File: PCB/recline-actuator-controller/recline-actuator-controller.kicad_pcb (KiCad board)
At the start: 4 copper layers, 140 x 100 mm, 171 parts, among them J1 DX07S016JA1R1500, J10 1757242, J11 1757242, J12 0705430002, J13 0705430002, J14 0705430002, J15 0705430002, J16 1757242, J17 1757242, J18 0705430002, J19 0705430002, J2 Conn_01x03, J20 0705430002, J21 0705430002, J22 1757242, J3 RJSAE-538A-02, J4 1757242, J5 1757242, J6 1757242, J7 1757242, J8 1757242, J9 1757242, M2 D24V22F3, Q1 PSMN7R0-60YS,115, Q2 PSMN7R0-60YS,115, Q3 PSMN7R0-60YS,115, Q4 PSMN7R0-60YS,115, Q5 PSMN7R0-60YS,115, Q6 BSC014N04LSIATMA1, Q7 BSC014N04LSIATMA1, Q8 BSC014N04LSIATMA1, Q9 BSC014N04LSIATMA1, SW1 TL3330AF260QG, SW2 TL3330AF260QG, U1 TEMPLATE, U2 RP2040, U3 MAX3535ECWI+T, U4 VNH5019ATR-E, U5 VNH5019ATR-E, U6 VNH5019ATR-E, U7 VNH5019ATR-E, U8 MCP23S17T-E/ML, X1 ABM8G-12.000MHZ-18-D2Y-T

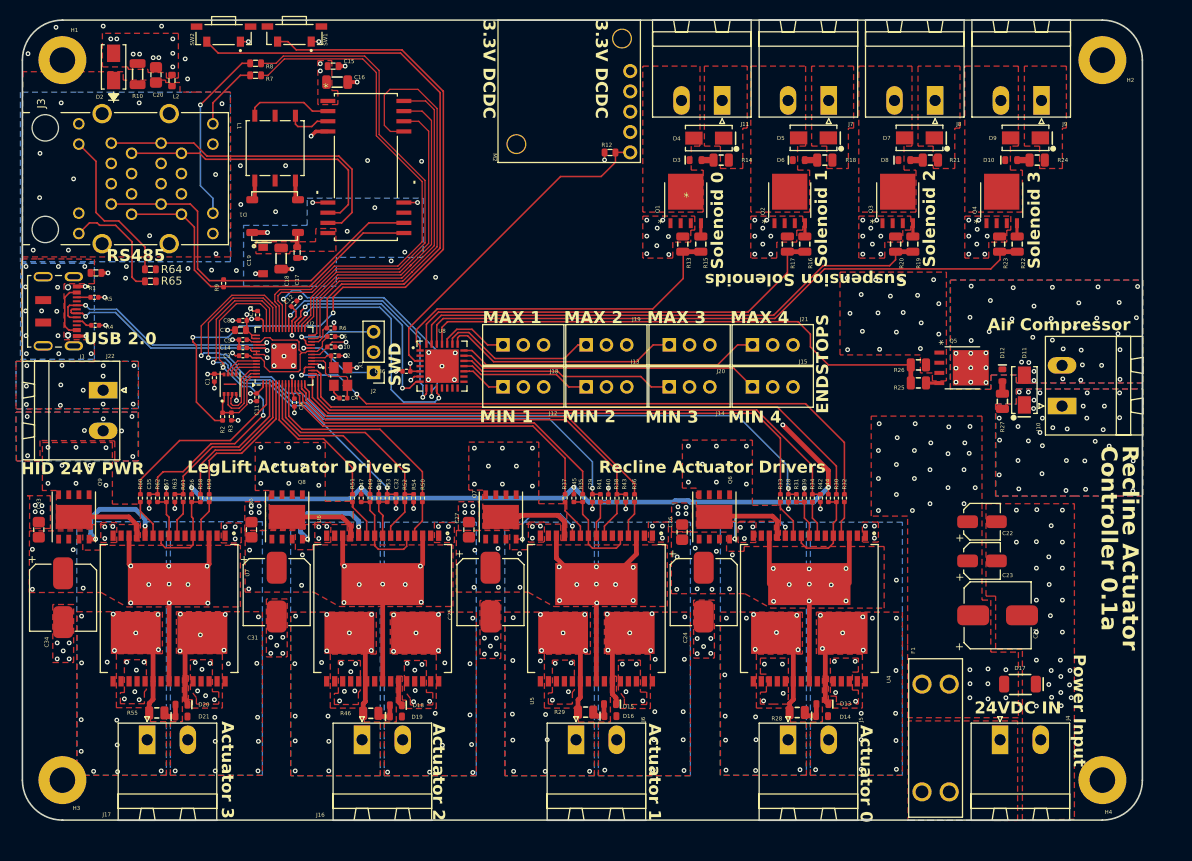
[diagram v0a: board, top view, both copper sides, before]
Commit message: Via Stichign and Pullups
Added optional pullups to endstop circuit.  Revised via stitching for input power, revised layout with added via stitching and copper pours for solenoid mosfets.
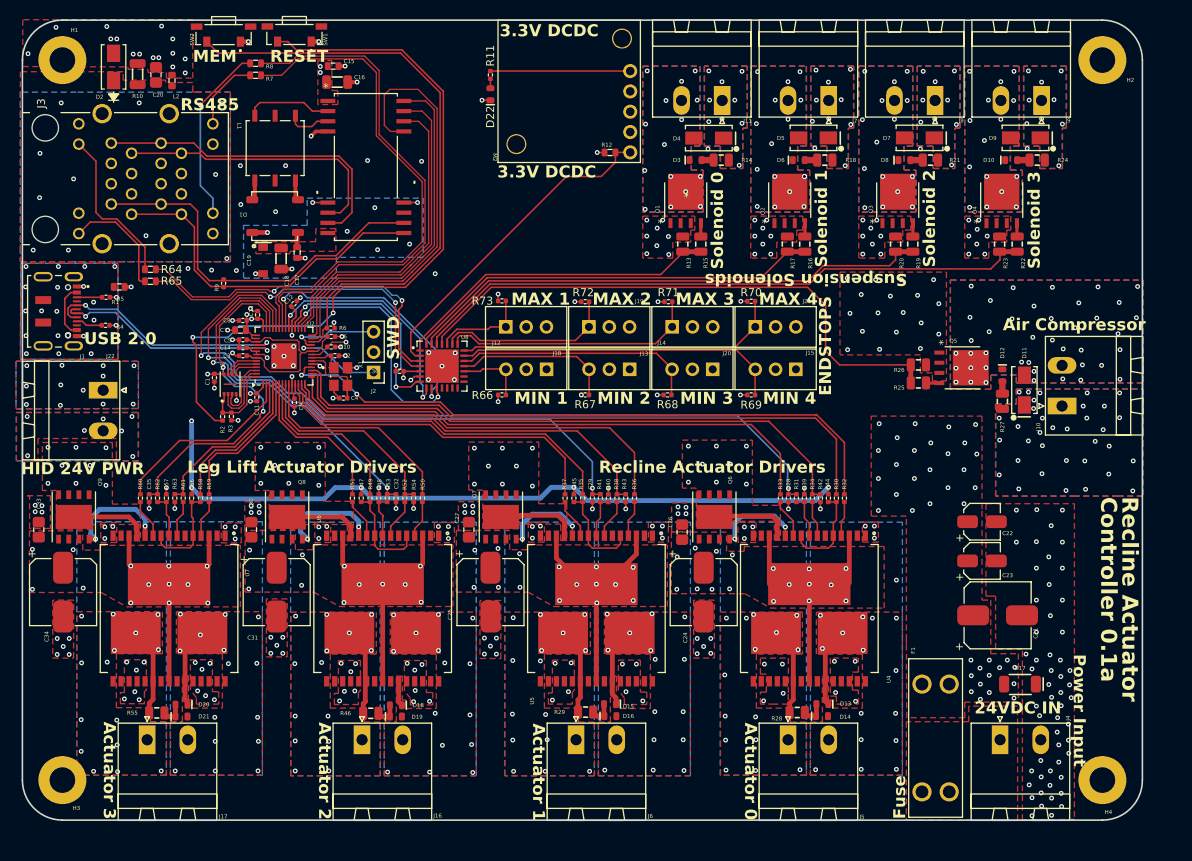
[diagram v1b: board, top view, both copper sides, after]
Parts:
- added D22: LTST-C194TBKT, AVR-KiCAD-Lib-Diodes:LED0603, F.Cu at (108.5, 54.3)
- added R11: RC0402FR-071KL, AVR-KiCAD-Lib-Resistors:R0402, F.Cu at (108.5, 51.9)
- added R66: RC0402FR-0710KL, AVR-KiCAD-Lib-Resistors:R0402, F.Cu at (110.0, 91.8)
- added R67: RC0402FR-0710KL, AVR-KiCAD-Lib-Resistors:R0402, F.Cu at (120.3, 91.8)
- added R68: RC0402FR-0710KL, AVR-KiCAD-Lib-Resistors:R0402, F.Cu at (130.7, 91.8)
- added R69: RC0402FR-0710KL, AVR-KiCAD-Lib-Resistors:R0402, F.Cu at (141.1, 91.8)
- added R70: RC0402FR-0710KL, AVR-KiCAD-Lib-Resistors:R0402, F.Cu at (141.1, 80.2)
- added R71: RC0402FR-0710KL, AVR-KiCAD-Lib-Resistors:R0402, F.Cu at (130.8, 80.2)
- added R72: RC0402FR-0710KL, AVR-KiCAD-Lib-Resistors:R0402, F.Cu at (120.3, 80.2)
- added R73: RC0402FR-0710KL, AVR-KiCAD-Lib-Resistors:R0402, F.Cu at (110.0, 80.1)
- moved J12 5.87 mm to (115.5, 88.7), turned to -90 degrees
- moved J13 5.87 mm to (125.9, 88.7), turned to -90 degrees
- moved J14 5.87 mm to (136.3, 88.7), turned to -90 degrees
- moved J15 5.87 mm to (146.7, 88.7), turned to -90 degrees
- moved R1 3.39 mm to (62.1, 78.3)
- moved J18 2.28 mm to (110.4, 83.3)
- moved J21 2.28 mm to (141.6, 83.3)
- moved J19 2.28 mm to (120.8, 83.3)
- moved J20 2.28 mm to (131.2, 83.3)
- moved R5 1.45 mm to (60.5, 79.7)
- moved R4 1.30 mm to (60.4, 83.2)
- moved C36 0.85 mm to (97.2, 88.9)
- moved C34 0.70 mm to (55.1, 116.5)
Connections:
- J12 pad 1: /End Stop Limit Switches/MIN1 -> +3.3V
- J12 pad 3: +3.3V -> /End Stop Limit Switches/MIN1
- J13 pad 1: /End Stop Limit Switches/MIN2 -> +3.3V
- J13 pad 3: +3.3V -> /End Stop Limit Switches/MIN2
- J14 pad 1: /End Stop Limit Switches/MIN3 -> +3.3V
- J14 pad 3: +3.3V -> /End Stop Limit Switches/MIN3
- J15 pad 1: /End Stop Limit Switches/MIN4 -> +3.3V
- J15 pad 3: +3.3V -> /End Stop Limit Switches/MIN4
- R64 pad 2: /RS485 Transceiver/RS485_TX_LED2 -> /End Stop Limit Switches/RS485_TX_LED2
- R65 pad 2: /RS485 Transceiver/RS485_RX_LED2 -> /End Stop Limit Switches/RS485_RX_LED2
- U8 pad 2: /End Stop Limit Switches/5V_PG -> /Power/3.3V_PG
- U8 pad 3: /Power/3.3V_PG -> /End Stop Limit Switches/RS485_TX_LED2
- U8 pad 4: unconnected-(U8-GPB7-Pad4) -> /End Stop Limit Switches/RS485_RX_LED2
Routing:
- net /End Stop Limit Switches/RS485_TX_LED2: track 0.00 -> 43.1 mm, vias 0 -> 2
- net /End Stop Limit Switches/RS485_RX_LED2: track 0.00 -> 42.4 mm, vias 0 -> 2
- net +3.3V: track 128.6 -> 150.4 mm, vias 19 -> 27
- net /End Stop Limit Switches/AIR_COMP: track 66.5 -> 71.8 mm
- net /End Stop Limit Switches/MIN2: track 16.4 -> 20.0 mm
- net /End Stop Limit Switches/MIN3: track 27.0 -> 30.4 mm
- net /End Stop Limit Switches/SOLENOID_0: track 44.4 -> 41.1 mm
- net /End Stop Limit Switches/MIN4: track 37.7 -> 40.9 mm
- net /End Stop Limit Switches/MAX4: track 37.8 -> 40.8 mm
- net /End Stop Limit Switches/MAX1: track 8.93 -> 11.9 mm
- net /End Stop Limit Switches/MIN1: track 5.69 -> 8.57 mm
- net /End Stop Limit Switches/SOLENOID_1: track 55.1 -> 52.5 mm
- net /End Stop Limit Switches/MAX2: track 19.8 -> 22.4 mm
- net /End Stop Limit Switches/MAX3: track 29.6 -> 32.2 mm
- net /Motor H-Bridges/M2INA: track 48.5 -> 50.8 mm
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- added copper zone on In1.Cu, net Net-(F1-Pad2)
- added copper zone on B.Cu, net Net-(Q1-D)
- added copper zone on In1.Cu, net Net-(Q1-D)
- added copper zone on B.Cu, net Net-(Q2-D)
- added copper zone on In1.Cu, net Net-(Q2-D)
- added copper zone on B.Cu, net Net-(Q3-D)
- added copper zone on In1.Cu, net Net-(Q3-D)
- added copper zone on B.Cu, net Net-(Q4-D)
- added copper zone on In1.Cu, net Net-(Q4-D)
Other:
- board text added: "3V3"
- board text added: "Fuse"
- board text added: "GPA0"
- board text added: "GPA1"
- board text added: "GPA2"
- board text added: "GPA3"
- board text added: "GPA4"
- board text added: "GPA5"
- board text added: "GPA6"
- board text added: "GPA7"
- board text added: "Leg Lift Actuator Drivers"
- board text added: "MEM"
- board text added: "NOTE: ALL ON IO EXPANDER"
- board text added: "RESET"
- board text removed: "LegLift Actuator Drivers"

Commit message: Powerplane
Recline actuator controller power plane topology modified and upgraded
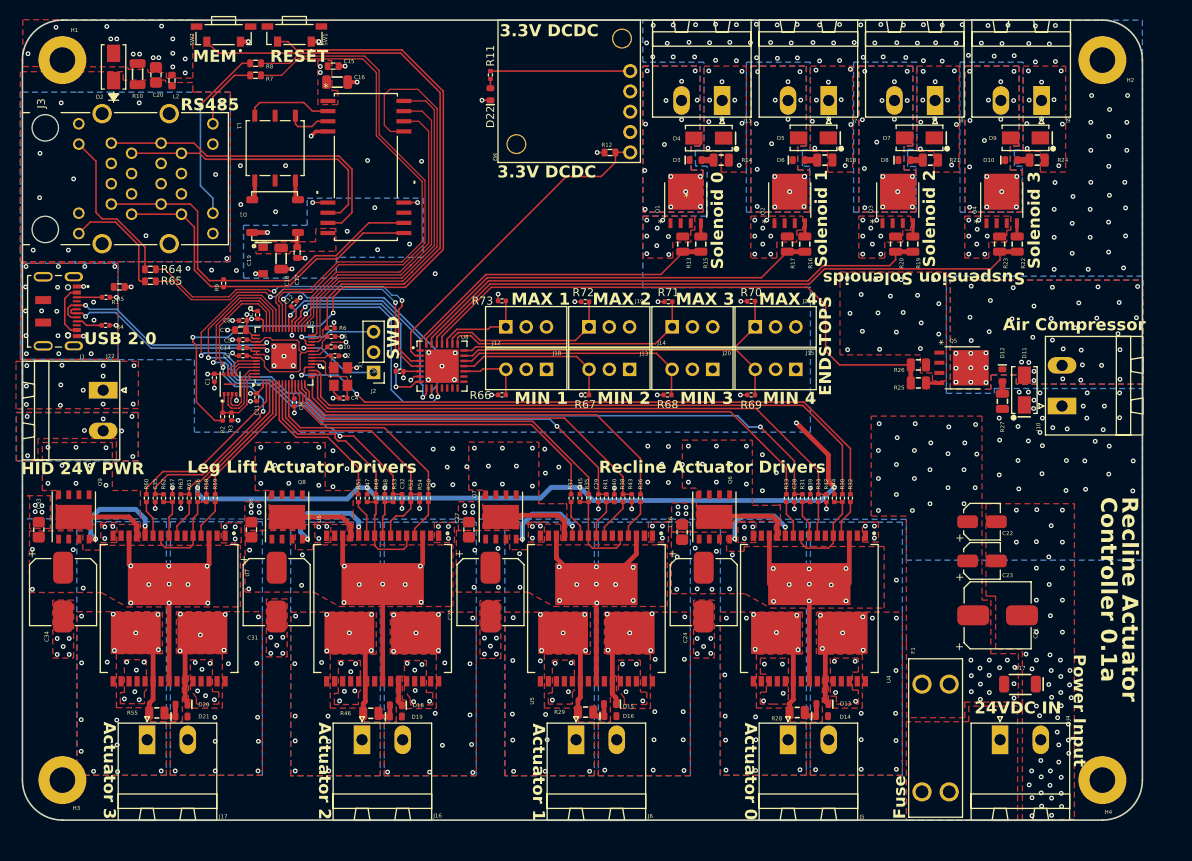
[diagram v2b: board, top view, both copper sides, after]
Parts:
- moved C28 0.75 mm to (146.5, 104.8)
- moved C29 0.75 mm to (122.0, 104.8)
- moved C32 0.75 mm to (97.5, 104.8)
- moved C35 0.75 mm to (66.6, 104.8)
- moved R30 0.75 mm to (152.5, 104.8)
- moved R31 0.75 mm to (147.5, 104.8)
- moved R32 0.75 mm to (153.5, 104.8)
- moved R33 0.75 mm to (145.5, 104.8)
- moved R34 0.75 mm to (149.5, 104.8)
- moved R35 0.75 mm to (120.8, 104.8)
- moved R36 0.75 mm to (127.3, 104.8)
- moved R37 0.75 mm to (118.6, 104.8)
- moved R38 0.75 mm to (125.1, 104.8)
- moved R39 0.75 mm to (148.5, 104.8)
- moved R40 0.75 mm to (124.0, 104.8)
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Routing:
- net +3.3V: track 150.4 -> 152.5 mm
- net /Leg Lift Motors/M4ENA/B: track 19.1 -> 17.3 mm
- net /Leg Lift Motors/M4INA: track 18.8 -> 17.0 mm
- net /Leg Lift Motors/M4PWM: track 21.0 -> 19.3 mm
- net /Leg Lift Motors/M3CS: track 46.3 -> 47.9 mm
- net /Leg Lift Motors/M4INB: track 23.8 -> 22.5 mm
- net /Motor H-Bridges/M1CS: track 101.9 -> 103.1 mm
- net /Leg Lift Motors/M3PWM: track 25.8 -> 26.7 mm
- net Net-(U6-PWM): track 4.95 -> 5.80 mm
- net /Leg Lift Motors/M3INA: track 26.5 -> 27.2 mm
- net +24V: vias 156 -> 264

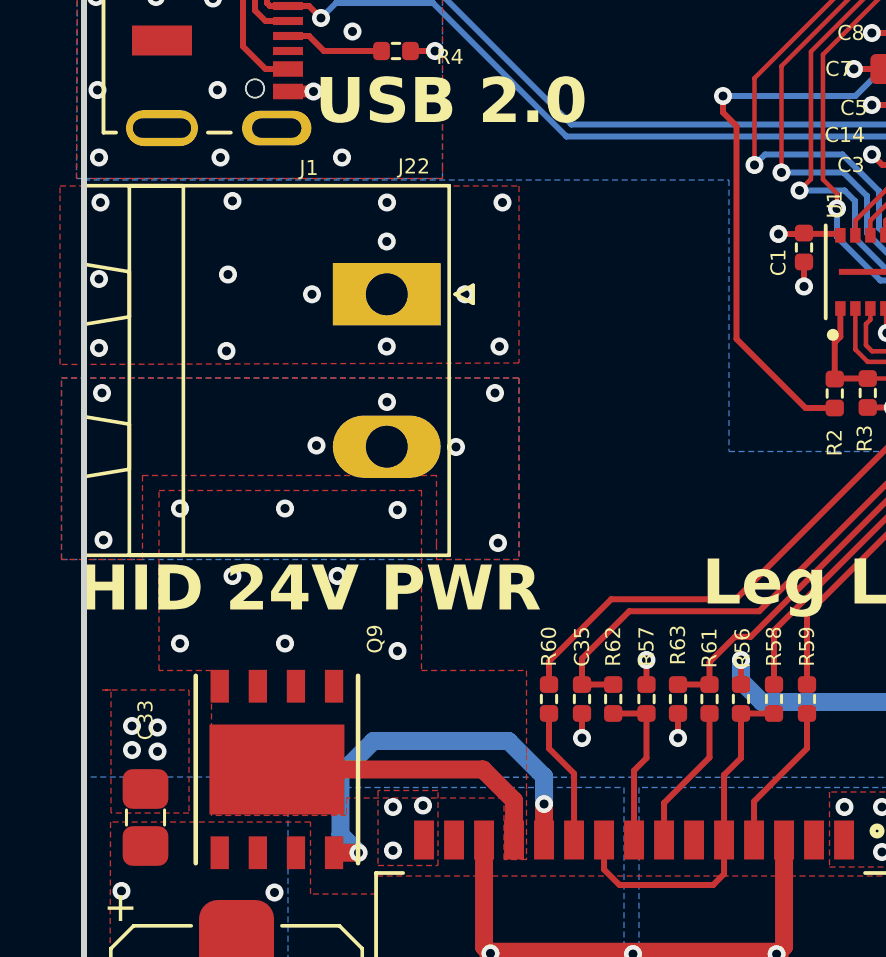
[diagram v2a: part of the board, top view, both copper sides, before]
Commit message: 3D Models
3D Models of circuit boards generated and added to project.
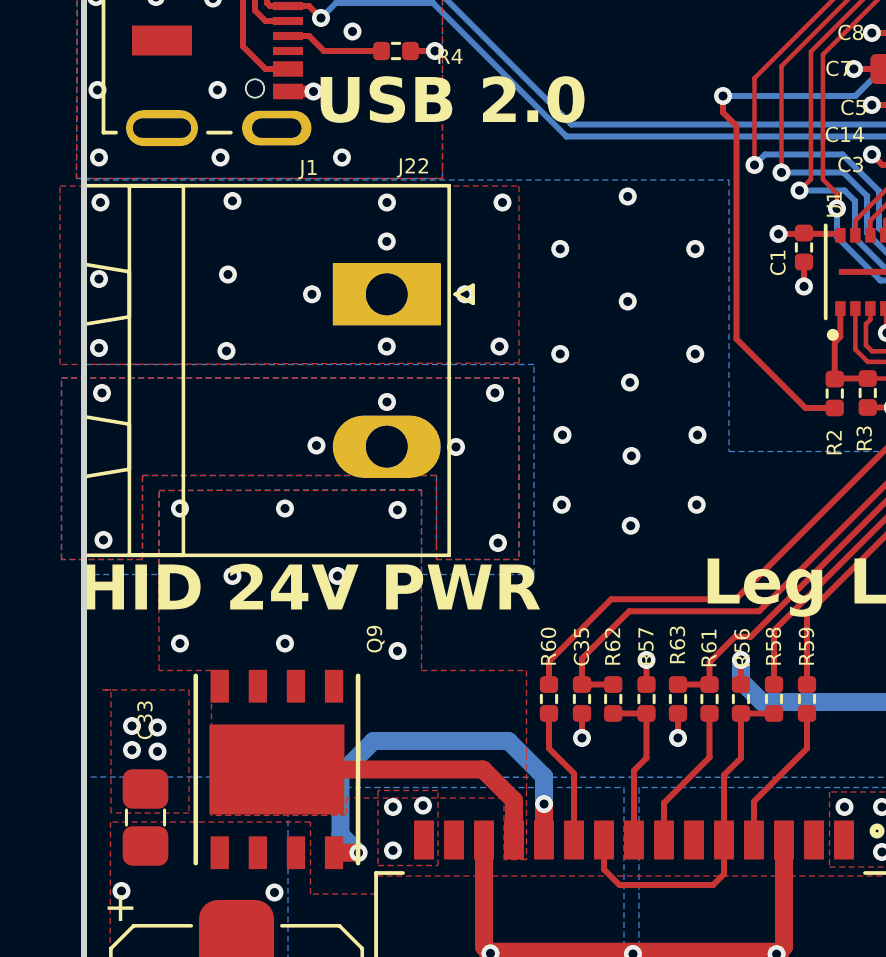
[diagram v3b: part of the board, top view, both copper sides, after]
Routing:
- net +24V: vias 264 -> 277
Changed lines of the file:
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@@
 	)
 	(via
+		(at 70.375 89.75)
+		(size 0.6)
+		(drill 0.3)
+		(layers "F.Cu" "B.Cu")
+		(net 8)
+	)
+	(via
+		(at 68.225 98.975)
+		(size 0.6)
+		(drill 0.3)
+		(layers "F.Cu" "B.Cu")
+		(net 8)
+	)
+	(via
 		(at 178.95 54.95)
 		(size 0.6)
@@
 	)
 	(via
+		(at 65.875 89.75)
+		(size 0.6)
+		(drill 0.3)
+		(layers "F.Cu" "B.Cu")
+		(net 8)
+	)
+	(via
 		(at 144.35 45.6)
 		(size 0.6)
@@
 	)
 	(via
+		(at 68.125 91.5)
+		(size 0.6)
+		(drill 0.3)
+		(layers "F.Cu" "B.Cu")
+		(net 8)
+	)
+	(via
 		(at 170.865 125)
 		(size 0.6)
@@
 	)
 	(via
+		(at 65.95 95.95)
+		(size 0.6)
+		(drill 0.3)
+		(layers "F.Cu" "B.Cu")
+		(net 8)
+	)
+	(via
 		(at 159.3 47.825)
 		(size 0.6)
@@
 	)
 	(via
+		(at 70.425 98.275)
+		(size 0.6)
+		(drill 0.3)
+		(layers "F.Cu" "B.Cu")
+		(net 8)
+	)
+	(via
 		(at 162.625 50.075)
 		(size 0.6)
@@
 	)
 	(via
+		(at 68.2 94.2)
+		(size 0.6)
+		(drill 0.3)
+		(layers "F.Cu" "B.Cu")
+		(net 8)
+	)
+	(via
 		(at 163.55 97.85)
 		(size 0.6)
@@
 	)
 	(via
+		(at 70.375 93.25)
+		(size 0.6)
+		(drill 0.3)
+		(layers "F.Cu" "B.Cu")
+		(net 8)
+	)
+	(via
 		(at 172.15 125.95)
 		(size 0.6)
@@
 	)
 	(via
+		(at 68.125 88)
+		(size 0.6)
+		(drill 0.3)
+		(layers "F.Cu" "B.Cu")
+		(net 8)
+	)
+	(via
 		(at 175.75 97.6)
 		(size 0.6)
@@
 	)
 	(via
+		(at 65.875 93.25)
+		(size 0.6)
+		(drill 0.3)
+		(layers "F.Cu" "B.Cu")
+		(net 8)
+	)
+	(via
 		(at 157.3 45.55)
 		(size 0.6)
@@
 	)
 	(via
+		(at 65.925 98.275)
+		(size 0.6)
+		(drill 0.3)
+		(layers "F.Cu" "B.Cu")
+		(net 8)
+	)
+	(via
 		(at 185.9 56.175)
 		(size 0.6)
@@
 	)
 	(via
+		(at 68.25 96.65)
+		(size 0.6)
+		(drill 0.3)
+		(layers "F.Cu" "B.Cu")
+		(net 8)
+	)
+	(via
 		(at 157 106.3)
 		(size 0.6)
@@
 	)
 	(via
+		(at 70.45 95.95)
+		(size 0.6)
+		(drill 0.3)
+		(layers "F.Cu" "B.Cu")
+		(net 8)
+	)
+	(via
 		(at 128.85 45.65)
 		(size 0.6)
@@
 			(pts
 				(xy 90.6 110.1) (xy 90.6 108.05) (xy 85.35 108.05) (xy 85.35 108.629614) (xy 80.85 108.629614) (xy 80.85 103.8)
-				(xy 79.1 103.8) (xy 79.1 97.8) (xy 87.85 97.8) (xy 87.85 103.8) (xy 87.85 103.8) (xy 91.35 103.8)
-				(xy 91.35 106.6) (xy 91.35 107.8) (xy 91.35 110.1)
+				(xy 79.1 103.8) (xy 79.1 97.8) (xy 87.85 97.8) (xy 87.85 103.8) (xy 91.35 103.8) (xy 91.35 106.6)
+				(xy 91.35 107.8) (xy 91.35 110.1)
 			)
 		)
@@
 			(pts
 				(xy 64 110.1) (xy 64 108.05) (xy 58.75 108.05) (xy 58.75 108.629614) (xy 54.25 108.629614) (xy 54.25 103.8)
-				(xy 52.5 103.8) (xy 52.5 97.8) (xy 61.25 97.8) (xy 61.25 103.8) (xy 61.25 103.8) (xy 64.75 103.8)
-				(xy 64.75 106.6) (xy 64.75 107.8) (xy 64.75 110.1)
+				(xy 52.5 103.8) (xy 52.5 97.8) (xy 61.25 97.8) (xy 61.25 103.8) (xy 64.75 103.8) (xy 64.75 106.6)
+				(xy 64.75 107.8) (xy 64.75 110.1)
 			)
 		)
@@
 		(polygon
 			(pts
-				(xy 49.25 94.05) (xy 64.5 94.05) (xy 64.5 100.1) (xy 49.25 100.1)
+				(xy 64.5 100.1) (xy 61.75 100.1) (xy 61.75 97.3) (xy 51.95 97.3) (xy 51.95 100.1) (xy 49.25 100.1)
+				(xy 49.25 94.05) (xy 64.5 94.05)
 			)
 		)
@@
 			(pts
 				(xy 190 76.35) (xy 190 77) (xy 165.5 77) (xy 165.5 91.05) (xy 165.5 91.65) (xy 171.5 91.65) (xy 171.5 91.05)
-				(xy 190 91.052631) (xy 190 112.5) (xy 160.5 112.5) (xy 160.5 107.4) (xy 50 107.35) (xy 50 87.45)
-				(xy 71.5 87.45) (xy 71.5 96.5) (xy 148.5 96.5) (xy 148.5 78.4) (xy 127.55 78.45) (xy 127.55 69.5)
+				(xy 190 91.052631) (xy 190 112.5) (xy 160.5 112.5) (xy 160.5 107.4) (xy 50 107.35) (xy 50 100.6)
+				(xy 52.5 100.6) (xy 52.5 97.8) (xy 61.25 97.775) (xy 61.25 100.6) (xy 65 100.6) (xy 65 93.6) (xy 50 93.6)
+				(xy 50 87.45) (xy 71.5 87.45) (xy 71.5 96.5) (xy 148.5 96.5) (xy 148.5 78.4) (xy 127.55 78.45) (xy 127.55 69.5)
 				(xy 135.6 69.5) (xy 135.6 63.25) (xy 134.15 63.25) (xy 134.1 61.25) (xy 135.2 61.25) (xy 135.2 50.25)
 				(xy 127.55 50.25) (xy 127.55 45) (xy 190 45)
